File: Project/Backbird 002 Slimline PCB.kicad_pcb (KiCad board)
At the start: 2 copper layers, 14 x 116 mm, 10 parts

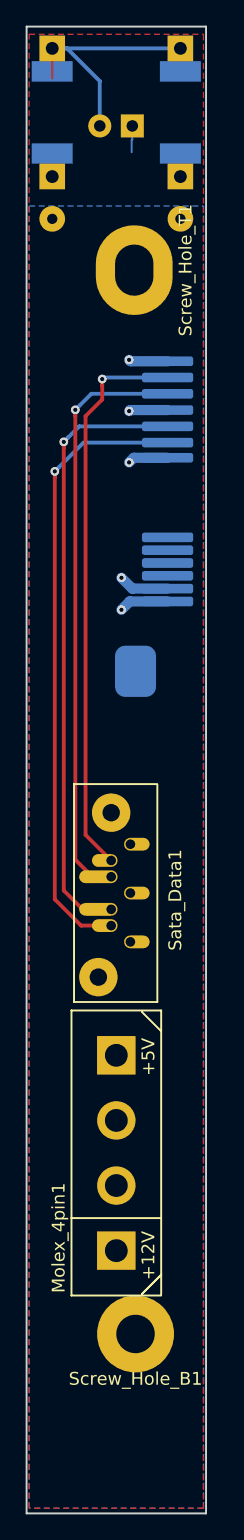
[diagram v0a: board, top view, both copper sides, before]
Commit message: Connected top components
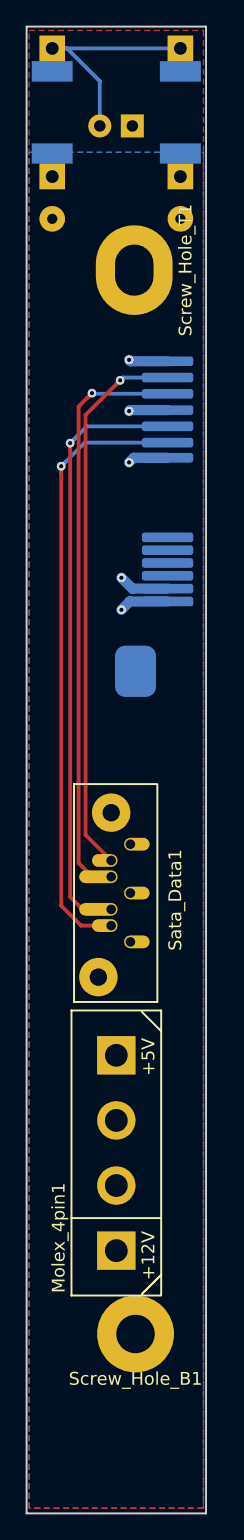
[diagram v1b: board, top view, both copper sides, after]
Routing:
- net Net-(D1-Pad2): track 20.6 -> 21.9 mm
- net A+: track 44.1 -> 43.2 mm
- net B-: track 48.6 -> 47.8 mm
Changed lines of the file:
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@@
     (thickness 1.6)
     (drawings 23)
-    (tracks 60)
+    (tracks 58)
     (zones 0)
     (modules 10)
@@
     (40 Dwgs.User user)
     (41 Cmts.User user)
-    (42 Eco1.User user)
-    (43 Eco2.User user)
+    (42 Eco1.User user hide)
+    (43 Eco2.User user hide)
     (44 Edge.Cuts user)
     (45 Margin user)
@@
   (gr_line (start 114.3 30.48) (end 114.3 146.48) (layer Eco1.User) (width 0.2))
   (gr_line (start 100.3 30.48) (end 114.3 30.48) (layer Eco1.User) (width 0.2))
-  (segment (start 102.3 32.17914) (end 102.3 34.52) (width 0.1524) (layer F.Cu) (net 1))
-  (segment (start 103.45189 32.17914) (end 102.3 32.17914) (width 0.3) (layer B.Cu) (net 1) (status 1000000))
-  (segment (start 106.01 38.23) (end 106.01 34.73725) (width 0.3) (layer B.Cu) (net 1) (status 1000000))
-  (segment (start 106.01 34.73725) (end 103.45189 32.17914) (width 0.3) (layer B.Cu) (net 1) (status 1000000))
+  (segment (start 103.45189 32.17914) (end 102.3 32.17914) (width 0.3) (layer B.Cu) (net 1))
+  (segment (start 106.01 38.23) (end 106.01 34.73725) (width 0.3) (layer B.Cu) (net 1))
+  (segment (start 106.01 34.73725) (end 103.45189 32.17914) (width 0.3) (layer B.Cu) (net 1))
   (segment (start 112.3 32.17914) (end 102.3 32.17914) (width 0.3) (layer B.Cu) (net 1))
+  (segment (start 102.3 32.17914) (end 102.3 33.98) (width 0.3) (layer B.Cu) (net 1))
+  (segment (start 112.3 32.17914) (end 112.3 33.98) (width 0.3) (layer B.Cu) (net 1))
   (segment (start 108.4 98.08) (end 109.4 98.08) (width 0.1524) (layer F.Cu) (net 2))
   (segment (start 108.4 101.89) (end 109.21 101.89) (width 0.1524) (layer F.Cu) (net 2))
   (segment (start 109.09 94.27) (end 108.4 94.27) (width 0.1524) (layer F.Cu) (net 2))
   (segment (start 107.3 115.880004) (end 107.3 115.82) (width 0.1524) (layer F.Cu) (net 2))
-  (segment (start 108.55 39.2824) (end 108.5 39.3324) (width 0.1524) (layer B.Cu) (net 2))
-  (segment (start 108.55 38.23) (end 108.55 39.2824) (width 0.1524) (layer B.Cu) (net 2))
-  (segment (start 108.5 39.3324) (end 108.5 40.28) (width 0.1524) (layer B.Cu) (net 2))
   (via (at 108.3 60.48) (size 0.6858) (drill 0.3302) (layers F.Cu B.Cu) (net 2))
   (segment (start 111.3 60.4) (end 108.38 60.4) (width 0.8) (layer B.Cu) (net 2))
@@
   (segment (start 107.7 75.98) (end 108.35 75.33) (width 0.8) (layer B.Cu) (net 2))
   (segment (start 108.35 75.33) (end 111.3 75.33) (width 0.8) (layer B.Cu) (net 2))
-  (via (at 102.5 65.18) (size 0.6858) (drill 0.3302) (layers F.Cu B.Cu) (net 5))
-  (segment (start 102.5 98.564933) (end 102.5 65.664933) (width 0.3) (layer F.Cu) (net 5))
-  (segment (start 102.5 65.664933) (end 102.5 65.18) (width 0.3) (layer F.Cu) (net 5))
+  (segment (start 112.3 40.3808) (end 112.3 42.18166) (width 0.3) (layer B.Cu) (net 2))
+  (segment (start 104.555067 100.62) (end 103 99.064933) (width 0.3) (layer F.Cu) (net 5))
   (segment (start 106.9 100.62) (end 104.555067 100.62) (width 0.3) (layer F.Cu) (net 5))
-  (segment (start 104.74 62.94) (end 102.842899 64.837101) (width 0.3) (layer B.Cu) (net 5))
-  (segment (start 104.555067 100.62) (end 102.5 98.564933) (width 0.3) (layer F.Cu) (net 5))
-  (segment (start 111.3 62.94) (end 104.74 62.94) (width 0.3) (layer B.Cu) (net 5))
-  (segment (start 102.842899 64.837101) (end 102.5 65.18) (width 0.3) (layer B.Cu) (net 5))
+  (segment (start 103.342899 64.437101) (end 103 64.78) (width 0.3) (layer B.Cu) (net 5))
+  (segment (start 104.84 62.94) (end 103.342899 64.437101) (width 0.3) (layer B.Cu) (net 5))
+  (segment (start 103 99.064933) (end 103 65.264933) (width 0.3) (layer F.Cu) (net 5))
+  (segment (start 111.3 62.94) (end 104.84 62.94) (width 0.3) (layer B.Cu) (net 5))
+  (segment (start 103 65.264933) (end 103 64.78) (width 0.3) (layer F.Cu) (net 5))
+  (via (at 103 64.78) (size 0.6858) (drill 0.3302) (layers F.Cu B.Cu) (net 5))
   (segment (start 106.9 99.35) (end 106.238934 99.35) (width 0.1524) (layer F.Cu) (net 6))
-  (via (at 103.199994 62.88) (size 0.6858) (drill 0.3302) (layers F.Cu B.Cu) (net 6))
-  (segment (start 104.409994 61.67) (end 103.542893 62.537101) (width 0.3) (layer B.Cu) (net 6))
-  (segment (start 104.67 99.35) (end 103.199994 97.879994) (width 0.3) (layer F.Cu) (net 6))
-  (segment (start 103.542893 62.537101) (end 103.199994 62.88) (width 0.3) (layer B.Cu) (net 6))
-  (segment (start 111.3 61.67) (end 104.409994 61.67) (width 0.3) (layer B.Cu) (net 6))
+  (via (at 103.700002 62.98) (size 0.6858) (drill 0.3302) (layers F.Cu B.Cu) (net 6))
+  (segment (start 105.010002 61.67) (end 104.042901 62.637101) (width 0.3) (layer B.Cu) (net 6))
+  (segment (start 111.3 61.67) (end 105.010002 61.67) (width 0.3) (layer B.Cu) (net 6))
+  (segment (start 104.042901 62.637101) (end 103.700002 62.98) (width 0.3) (layer B.Cu) (net 6))
+  (segment (start 104.67 99.35) (end 103.700002 98.380002) (width 0.3) (layer F.Cu) (net 6))
   (segment (start 106.9 99.35) (end 104.67 99.35) (width 0.3) (layer F.Cu) (net 6))
-  (segment (start 103.199994 97.879994) (end 103.199994 63.364933) (width 0.3) (layer F.Cu) (net 6))
-  (segment (start 103.199994 63.364933) (end 103.199994 62.88) (width 0.3) (layer F.Cu) (net 6))
-  (segment (start 104.1 60.864933) (end 104.1 60.38) (width 0.3) (layer F.Cu) (net 7))
-  (segment (start 104.1 95.48) (end 104.1 60.864933) (width 0.3) (layer F.Cu) (net 7))
+  (segment (start 103.700002 98.380002) (end 103.700002 63.464933) (width 0.3) (layer F.Cu) (net 6))
+  (segment (start 103.700002 63.464933) (end 103.700002 62.98) (width 0.3) (layer F.Cu) (net 6))
+  (via (at 105.4 59.08) (size 0.6858) (drill 0.3302) (layers F.Cu B.Cu) (net 7))
+  (segment (start 105.43 96.81) (end 104.357101 95.737101) (width 0.3) (layer F.Cu) (net 7))
+  (segment (start 111.3 59.13) (end 105.45 59.13) (width 0.3) (layer B.Cu) (net 7))
+  (segment (start 104.357101 95.737101) (end 104.357101 60.122899) (width 0.3) (layer F.Cu) (net 7))
+  (segment (start 104.357101 60.122899) (end 105.057101 59.422899) (width 0.3) (layer F.Cu) (net 7))
+  (segment (start 105.057101 59.422899) (end 105.4 59.08) (width 0.3) (layer F.Cu) (net 7))
+  (segment (start 105.45 59.13) (end 105.4 59.08) (width 0.3) (layer B.Cu) (net 7))
   (segment (start 106.9 96.81) (end 105.43 96.81) (width 0.3) (layer F.Cu) (net 7))
-  (segment (start 105.43 96.81) (end 104.1 95.48) (width 0.3) (layer F.Cu) (net 7))
-  (segment (start 104.442899 60.037101) (end 104.1 60.38) (width 0.3) (layer B.Cu) (net 7))
-  (segment (start 105.35 59.13) (end 104.442899 60.037101) (width 0.3) (layer B.Cu) (net 7))
-  (via (at 104.1 60.38) (size 0.6858) (drill 0.3302) (layers F.Cu B.Cu) (net 7))
-  (segment (start 111.3 59.13) (end 105.35 59.13) (width 0.3) (layer B.Cu) (net 7))
-  (segment (start 106.319998 57.86) (end 106.2 57.979998) (width 0.3) (layer B.Cu) (net 8))
-  (segment (start 111.3 57.86) (end 106.319998 57.86) (width 0.3) (layer B.Cu) (net 8))
-  (via (at 106.2 57.979998) (size 0.6858) (drill 0.3302) (layers F.Cu B.Cu) (net 8))
-  (segment (start 106.2 59.575865) (end 106.2 58.464931) (width 0.3) (layer F.Cu) (net 8))
-  (segment (start 104.9 60.875865) (end 106.2 59.575865) (width 0.3) (layer F.Cu) (net 8))
+  (via (at 107.599992 58.08) (size 0.6858) (drill 0.3302) (layers F.Cu B.Cu) (net 8))
+  (segment (start 107.819992 57.86) (end 107.599992 58.08) (width 0.3) (layer B.Cu) (net 8))
+  (segment (start 111.3 57.86) (end 107.819992 57.86) (width 0.3) (layer B.Cu) (net 8))
   (segment (start 106.9 95.54) (end 104.9 93.54) (width 0.3) (layer F.Cu) (net 8))
-  (segment (start 106.2 58.464931) (end 106.2 57.979998) (width 0.3) (layer F.Cu) (net 8))
-  (segment (start 104.9 93.54) (end 104.9 60.875865) (width 0.3) (layer F.Cu) (net 8))
+  (segment (start 107.257093 58.422899) (end 107.599992 58.08) (width 0.3) (layer F.Cu) (net 8))
+  (segment (start 104.9 93.54) (end 104.9 60.779992) (width 0.3) (layer F.Cu) (net 8))
+  (segment (start 104.9 60.779992) (end 107.257093 58.422899) (width 0.3) (layer F.Cu) (net 8))
   (zone (net 3) (net_name +5V) (layer B.Cu) (hatch edge 0.508)
     (connect_pads (clearance 0.508))
@@
     (polygon
       (pts
-        (xy 100.5 44.48) (xy 114.1 44.48) (xy 114.1 146.08) (xy 100.5 146.08)
+        (xy 100.5 40.28) (xy 114.1 40.28) (xy 114.1 146.08) (xy 100.5 146.08)
       )
     )
@@
     (polygon
       (pts
-        (xy 100.5 31.08) (xy 114.1 31.08) (xy 114.1 146.08) (xy 100.5 146.08)
+        (xy 100.5 30.78) (xy 114.1 30.78) (xy 114.1 146.08) (xy 100.5 146.08)
       )
     )

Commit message: Edited receptacle so that the origin of the pads are lower instead of in the center
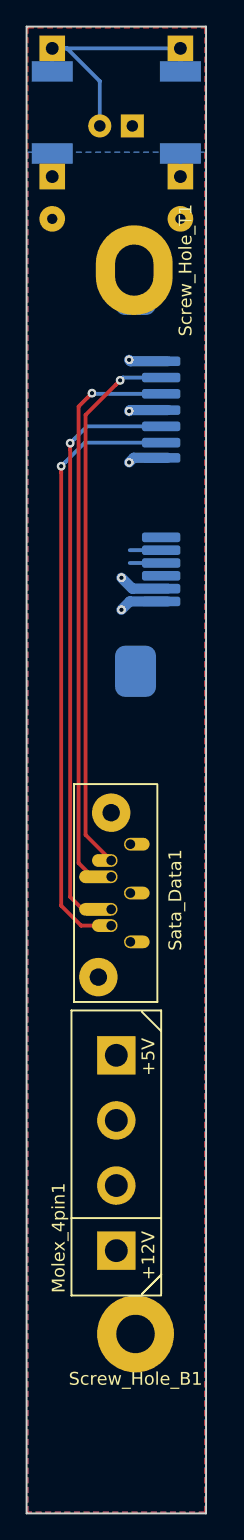
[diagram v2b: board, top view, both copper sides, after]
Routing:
- net +5V: track 0.00 -> 2.90 mm
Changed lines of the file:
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@@
     (thickness 1.6)
     (drawings 23)
-    (tracks 58)
+    (tracks 60)
     (zones 0)
     (modules 10)
@@
   (page A4)
   (layers
-    (0 F.Cu signal)
+    (0 F.Cu signal hide)
     (31 B.Cu signal)
     (32 B.Adhes user)
@@
     (fp_line (start -3.5 2) (end 0.5 2) (layer B.SilkS) (width 0.15))
     (fp_line (start 14.7 -3) (end -14.7 -3) (layer B.SilkS) (width 0.15))
-    (pad "" smd roundrect (at 14.9 0 90) (size 2 3.2) (layers B.Cu B.Paste B.Mask) (roundrect_rratio 0.25))
+    (pad 1 smd roundrect (at 9.29 1 90) (size 0.75 3) (drill (offset 0 1)) (layers B.Cu B.Paste B.Mask) (roundrect_rratio 0.25)
+      (net 2 GND))
+    (pad 2 smd roundrect (at 8.02 1 90) (size 0.75 3) (drill (offset 0 1)) (layers B.Cu B.Paste B.Mask) (roundrect_rratio 0.25)
+      (net 8 A+))
+    (pad 3 smd roundrect (at 6.75 1 90) (size 0.75 3) (drill (offset 0 1)) (layers B.Cu B.Paste B.Mask) (roundrect_rratio 0.25)
+      (net 7 A-))
+    (pad 4 smd roundrect (at 5.48 1 90) (size 0.75 3) (drill (offset 0 1)) (layers B.Cu B.Paste B.Mask) (roundrect_rratio 0.25)
+      (net 2 GND))
+    (pad 5 smd roundrect (at 4.21 1 90) (size 0.75 3) (drill (offset 0 1)) (layers B.Cu B.Paste B.Mask) (roundrect_rratio 0.25)
+      (net 6 B-))
+    (pad 6 smd roundrect (at 2.94 1 90) (size 0.75 3) (drill (offset 0 1)) (layers B.Cu B.Paste B.Mask) (roundrect_rratio 0.25)
+      (net 5 B+))
+    (pad 7 smd roundrect (at 1.75 1 90) (size 0.75 3) (drill (offset 0 1)) (layers B.Cu B.Paste B.Mask) (roundrect_rratio 0.25)
+      (net 2 GND))
+    (pad 8 smd roundrect (at -4.45 1 90) (size 0.75 3) (drill (offset 0 1)) (layers B.Cu B.Paste B.Mask) (roundrect_rratio 0.25)
+      (net 10 "Net-(Sata_Slimline_Recpt1-Pad8)"))
+    (pad 9 smd roundrect (at -5.45 1 90) (size 0.75 3) (drill (offset 0 1)) (layers B.Cu B.Paste B.Mask) (roundrect_rratio 0.25)
+      (net 3 +5V))
+    (pad 10 smd roundrect (at -6.45 1 90) (size 0.75 3) (drill (offset 0 1)) (layers B.Cu B.Paste B.Mask) (roundrect_rratio 0.25)
+      (net 3 +5V))
+    (pad 11 smd roundrect (at -7.45 1 90) (size 0.75 3) (drill (offset 0 1)) (layers B.Cu B.Paste B.Mask) (roundrect_rratio 0.25)
+      (net 9 "Net-(Sata_Slimline_Recpt1-Pad11)"))
+    (pad 12 smd roundrect (at -8.45 1 90) (size 0.75 3) (drill (offset 0 1)) (layers B.Cu B.Paste B.Mask) (roundrect_rratio 0.25)
+      (net 2 GND))
+    (pad "" smd roundrect (at 14.9 0 90) (size 4 3.2) (layers B.Cu B.Paste B.Mask) (roundrect_rratio 0.25))
     (pad "" smd roundrect (at -14.9 0 90) (size 4 3.2) (layers B.Cu B.Paste B.Mask) (roundrect_rratio 0.25))
-    (pad 7 smd roundrect (at 1.76 2.5 90) (size 0.75 4) (layers B.Cu B.Paste B.Mask) (roundrect_rratio 0.25)
-      (net 2 GND))
-    (pad 6 smd roundrect (at 2.94 2.5 90) (size 0.75 4) (layers B.Cu B.Paste B.Mask) (roundrect_rratio 0.25)
-      (net 5 B+))
-    (pad 5 smd roundrect (at 4.21 2.5 90) (size 0.75 4) (layers B.Cu B.Paste B.Mask) (roundrect_rratio 0.25)
-      (net 6 B-))
-    (pad 4 smd roundrect (at 5.48 2.5 90) (size 0.75 4) (layers B.Cu B.Paste B.Mask) (roundrect_rratio 0.25)
-      (net 2 GND))
-    (pad 3 smd roundrect (at 6.75 2.5 90) (size 0.75 4) (layers B.Cu B.Paste B.Mask) (roundrect_rratio 0.25)
-      (net 7 A-))
-    (pad 2 smd roundrect (at 8.02 2.5 90) (size 0.75 4) (layers B.Cu B.Paste B.Mask) (roundrect_rratio 0.25)
-      (net 8 A+))
-    (pad 1 smd roundrect (at 9.29 2.5 90) (size 0.75 4) (layers B.Cu B.Paste B.Mask) (roundrect_rratio 0.25)
-      (net 2 GND))
-    (pad 8 smd roundrect (at -4.45 2.5 90) (size 0.75 4) (layers B.Cu B.Paste B.Mask) (roundrect_rratio 0.25)
-      (net 10 "Net-(Sata_Slimline_Recpt1-Pad8)"))
-    (pad 9 smd roundrect (at -5.45 2.5 90) (size 0.75 4) (layers B.Cu B.Paste B.Mask) (roundrect_rratio 0.25)
-      (net 3 +5V))
-    (pad 10 smd roundrect (at -6.45 2.5 90) (size 0.75 4) (layers B.Cu B.Paste B.Mask) (roundrect_rratio 0.25)
-      (net 3 +5V))
-    (pad 11 smd roundrect (at -7.45 2.5 90) (size 0.75 4) (layers B.Cu B.Paste B.Mask) (roundrect_rratio 0.25)
-      (net 9 "Net-(Sata_Slimline_Recpt1-Pad11)"))
-    (pad 12 smd roundrect (at -8.45 2.5 90) (size 0.75 4) (layers B.Cu B.Paste B.Mask) (roundrect_rratio 0.25)
-      (net 2 GND))
-    (pad 13 smd roundrect (at -9.45 2.5 90) (size 0.75 4) (layers B.Cu B.Paste B.Mask) (roundrect_rratio 0.25)
+    (pad 13 smd roundrect (at -9.45 1 90) (size 0.75 3) (drill (offset 0 1)) (layers B.Cu B.Paste B.Mask) (roundrect_rratio 0.25)
       (net 2 GND))
   )
@@
   (segment (start 108.35 75.33) (end 111.3 75.33) (width 0.8) (layer B.Cu) (net 2))
   (segment (start 112.3 40.3808) (end 112.3 42.18166) (width 0.3) (layer B.Cu) (net 2))
+  (segment (start 109.8 71.33) (end 108.35 71.33) (width 0.3) (layer B.Cu) (net 3))
+  (segment (start 109.8 72.33) (end 108.35 72.33) (width 0.3) (layer B.Cu) (net 3))
   (segment (start 104.555067 100.62) (end 103 99.064933) (width 0.3) (layer F.Cu) (net 5))
   (segment (start 106.9 100.62) (end 104.555067 100.62) (width 0.3) (layer F.Cu) (net 5))
@@
     (polygon
       (pts
-        (xy 100.5 40.28) (xy 114.1 40.28) (xy 114.1 146.08) (xy 100.5 146.08)
+        (xy 100.4 40.28) (xy 114.2 40.28) (xy 114.2 146.38) (xy 100.4 146.38)
       )
     )
@@
     (polygon
       (pts
-        (xy 100.5 30.78) (xy 114.1 30.78) (xy 114.1 146.08) (xy 100.5 146.08)
+        (xy 100.4 30.58) (xy 114.2 30.58) (xy 114.2 146.38) (xy 100.4 146.38)
       )
     )

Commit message: remove extra 2 holes for the LED section
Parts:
- removed +5V_Hole1, GND_Hole2: Conn_01x01, Wire_Pads:SolderWirePad_single_0-8mmDrill
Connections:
- net +12V renamed Net-(Molex_4pin1-Pad1)
